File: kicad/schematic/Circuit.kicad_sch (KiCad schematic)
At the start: 54 parts, among them M1 Motor_DC, M2 Motor_DC, M3 Motor_DC, M4 Motor_DC, M5 Motor_DC, M6 Motor_DC, M7 Motor_DC, M8 Motor_DC, Q1 AO3400A, Q2 AO3400A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

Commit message: changed board layout. WIP
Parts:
- added BAT+1, BAT-1, RGB-DIN1, RGB-VDD1, RGB-gnd1, m1+1, m1-1, m2+1, m2-1, m3+1, m3-1, m4+1, m4-1, m5+1, m5-1, m6+1, m6-1, m7+1, m7-1, m8+1, m8-1: ~, ESP_global:blank pad, symbol waveshare_esp32_s3_mini_zero:blank_pad_1
- added C9: C_Polarized, Capacitor_SMD:CP_Elec_8x10.5, symbol Device:C_Polarized
- added D9: WS2812B, LED_SMD:LED_WS2812B_PLCC4_5.0x5.0mm_P3.2mm, symbol LED:WS2812B
- added H1: MountingHole_Pad, symbol Mechanical:MountingHole_Pad
- added R19: R, Resistor_SMD:R_0805_2012Metric, symbol Device:R
- added SW1: SW_Push, symbol Switch:SW_Push
- added TP1, TP2: TestPoint, symbol Connector:TestPoint
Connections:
- net GND: now also C9.2, D9.3 (VSS), RGB-gnd1.1 (pin)
- net at C1.2, C2.2, C3.2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: now also SW1.2, TP1.1, m1+1.1 (pin), m2+1.1 (pin), m3+1.1 (pin), m4+1.1 (pin), m5+1.1 (pin), m6+1.1 (pin), m7+1.1 (pin), m8+1.1 (pin); no longer U1.5 (OUT+)
- net at C2.1, D2.2 (A), M2.2 (-)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: now also m2-1.1 (pin)
- net at BT1.1 (+), U1.2 (Battery+): now also BAT+1.1 (pin)
- net at BT1.2 (-), U1.3 (Battery-): now also BAT-1.1 (pin)
- net at C8.1, D8.2 (A), M8.2 (-)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: now also m8-1.1 (pin)
- net at Q3.1 (G), R4.1: no longer R9.1
- net at C4.1, D4.2 (A), M4.2 (-)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: now also m4-1.1 (pin)
- net at ESP32_S3_ZERO1.13 (GP10), R4.2: now also R9.1
- net at Q6.1 (G), R11.1: no longer R12.1
- net at C6.1, D6.2 (A), M6.2 (-)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: now also m6-1.1 (pin)
- net at Q7.1 (G), R13.1: no longer R14.1
- net at C5.1, D5.2 (A), M5.2 (-)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: now also m5-1.1 (pin)
- net at Q4.1 (G), R5.1: no longer R10.1
- net at ESP32_S3_ZERO1.12 (GP9), R5.2: now also R10.1
- net at Q8.1 (G), R15.1: no longer R16.1
- net at ESP32_S3_ZERO1.9 (GP6), R15.2: now also R16.1
- net at Q5.1 (G), R1.1: no longer R6.1
- net at C1.1, D1.2 (A), M1.2 (-)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: now also m1-1.1 (pin)
- net at Q1.1 (G), R2.1: no longer R7.1
- net at ESP32_S3_ZERO1.15 (GP12), R2.2: now also R7.1
- net at ESP32_S3_ZERO1.1 (5V), R17.1, U2.1 (OUT_+): now also C9.1, D9.1 (VDD), RGB-VDD1.1 (pin)
- net at C7.1, D7.2 (A), M7.2 (-)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: now also m7-1.1 (pin)
- net at Q2.1 (G), R3.1: no longer R8.1
- net at C3.1, D3.2 (A), M3.2 (-)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: now also m3-1.1 (pin)
- net at ESP32_S3_ZERO1.10 (GP7), R13.2: now also R14.1
- net at ESP32_S3_ZERO1.16 (GP13), R1.2: now also R6.1
- net at ESP32_S3_ZERO1.11 (GP8), R11.2: now also R12.1
- net at ESP32_S3_ZERO1.14 (GP11), R3.2: now also R8.1
- net at ESP32_S3_ZERO1.8 (GP5): now also R19.1
- new net: D9.4 (DIN), R19.2, RGB-DIN1.1 (pin)
- new net: SW1.1, TP2.1, U1.5 (OUT+)
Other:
- moved on the sheet: ESP32_S3_ZERO1, R1, R10, R11, R12, R13, R14, R15, R16, R2, R3, R4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

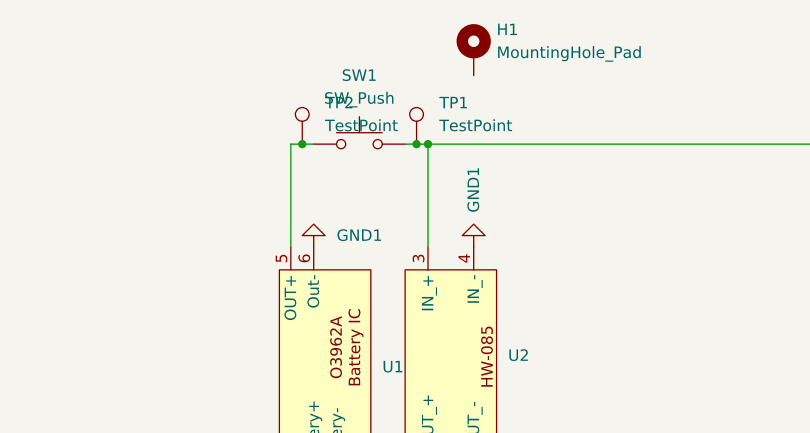
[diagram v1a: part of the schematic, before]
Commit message: upgedatetes Schematic hinzugefuegt
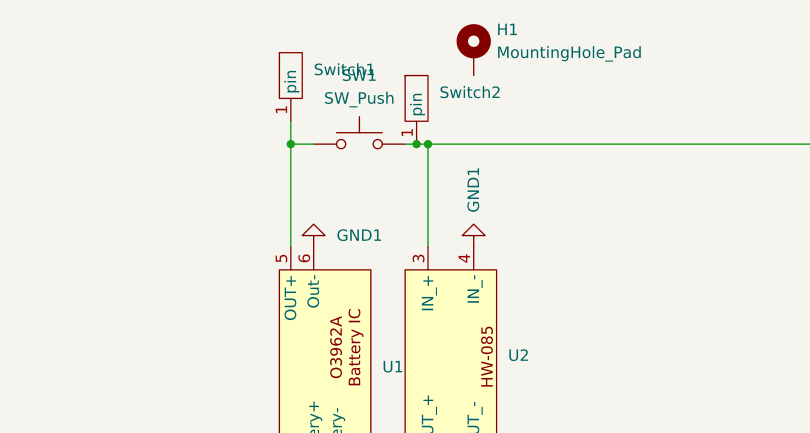
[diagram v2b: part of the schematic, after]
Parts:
- removed TP1, TP2: TestPoint, symbol Connector:TestPoint
- added Switch1, Switch2: ~, ESP_global:blank pad, symbol waveshare_esp32_s3_mini_zero:blank_pad_1
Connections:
- net at C1.2, C2.2, C3.2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: now also Switch2.1 (pin)
- net at SW1.1, U1.5 (OUT+): now also Switch1.1 (pin)
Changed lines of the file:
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@@
 	)
 	(junction
+		(at 143.51 46.99)
+		(diameter 0)
+		(color 0 0 0 0)
+	)
+	(junction
 		(at 289.56 106.68)
 		(diameter 0)
@@
 	)
 	(junction
-		(at 157.48 46.99)
-		(diameter 0)
-		(color 0 0 0 0)
-	)
-	(junction
 		(at 289.56 172.72)
 		(diameter 0)
@@
 	)
 	(junction
-		(at 144.78 46.99)
-		(diameter 0)
-		(color 0 0 0 0)
-	)
-	(junction
 		(at 234.95 182.88)
 		(diameter 0)
@@
 	)
 	(junction
+		(at 157.48 46.99)
+		(diameter 0)
+		(color 0 0 0 0)
+	)
+	(junction
 		(at 278.13 142.24)
 		(diameter 0)
@@
 	(wire
 		(pts
-			(xy 144.78 46.99) (xy 146.05 46.99)
+			(xy 143.51 46.99) (xy 146.05 46.99)
 		)
 		(stroke
@@
 	(wire
 		(pts
+			(xy 157.48 46.99) (xy 158.75 46.99)
+		)
+		(stroke
+			(width 0)
+			(type default)
+		)
+	)
+	(wire
+		(pts
 			(xy 278.13 187.96) (xy 278.13 190.5)
 		)
@@
 	(wire
 		(pts
-			(xy 143.51 46.99) (xy 144.78 46.99)
-		)
-		(stroke
-			(width 0)
-			(type default)
-		)
-	)
-	(wire
-		(pts
 			(xy 236.22 57.15) (xy 238.76 57.15)
 		)
@@
 	(wire
 		(pts
-			(xy 143.51 58.42) (xy 143.51 46.99)
-		)
-		(stroke
-			(width 0)
-			(type default)
-		)
-	)
-	(wire
-		(pts
 			(xy 278.13 71.12) (xy 278.13 73.66)
 		)
@@
 	(wire
 		(pts
+			(xy 143.51 46.99) (xy 143.51 58.42)
+		)
+		(stroke
+			(width 0)
+			(type default)
+		)
+	)
+	(wire
+		(pts
 			(xy 269.24 71.12) (xy 265.43 71.12)
 		)
@@
 	(wire
 		(pts
+			(xy 143.51 44.45) (xy 143.51 46.99)
+		)
+		(stroke
+			(width 0)
+			(type default)
+		)
+	)
+	(wire
+		(pts
 			(xy 255.27 137.16) (xy 269.24 137.16)
 		)
@@
 		)
 	)
-	(wire
-		(pts
-			(xy 157.48 46.99) (xy 158.75 46.99)
-		)
-		(stroke
-			(width 0)
-			(type default)
-		)
-	)
 	(symbol
 		(lib_id "power:GND")
@@
 	)
 	(symbol
-		(lib_id "Connector:TestPoint")
-		(at 144.78 46.99 0)
-		(unit 1)
-		(exclude_from_sim no)
-		(in_bom yes)
-		(on_board yes)
-		(dnp no)
-		(fields_autoplaced yes)
-		(property "Reference" "TP2"
-			(at 147.32 42.4179 0)
-			(effects
-				(font
-					(size 1.27 1.27)
-				)
-				(justify left)
-			)
-		)
-		(property "Value" "TestPoint"
-			(at 147.32 44.9579 0)
-			(effects
-				(font
-					(size 1.27 1.27)
-				)
-				(justify left)
-			)
-		)
-		(property "Footprint" ""
-			(at 149.86 46.99 0)
-			(effects
-				(font
-					(size 1.27 1.27)
-				)
-				(hide yes)
-			)
-		)
-		(property "Datasheet" "~"
-			(at 149.86 46.99 0)
-			(effects
-				(font
-					(size 1.27 1.27)
-				)
-				(hide yes)
-			)
-		)
-		(property "Description" "test point"
-			(at 144.78 46.99 0)
-			(effects
-				(font
-					(size 1.27 1.27)
-				)
-				(hide yes)
-			)
-		)
-		(pin "1"
-		)
-		(instances
-			(project "Circuit"
-				(path "/b1011026-c160-485a-bf1a-9bf26ac94018"
-					(reference "TP2")
-					(unit 1)
-				)
-			)
-		)
-	)
-	(symbol
 		(lib_id "Device:C")
 		(at 269.24 58.42 180)
@@
 	)
 	(symbol
+		(lib_id "waveshare_esp32_s3_mini_zero:blank_pad_1")
+		(at 143.51 39.37 0)
+		(unit 1)
+		(exclude_from_sim no)
+		(in_bom yes)
+		(on_board yes)
+		(dnp no)
+		(fields_autoplaced yes)
+		(property "Reference" "Switch1"
+			(at 146.05 38.7349 0)
+			(effects
+				(font
+					(size 1.27 1.27)
+				)
+				(justify left)
+			)
+		)
+		(property "Value" "~"
+			(at 146.05 40.64 0)
+			(effects
+				(font
+					(size 1.27 1.27)
+				)
+				(justify left)
+			)
+		)
+		(property "Footprint" "ESP_global:blank pad"
+			(at 143.51 39.37 0)
+			(effects
+				(font
+					(size 1.27 1.27)
+				)
+				(hide yes)
+			)
+		)
+		(property "Datasheet" ""
+			(at 143.51 39.37 0)
+			(effects
+				(font
+					(size 1.27 1.27)
+				)
+				(hide yes)
+			)
+		)
+		(property "Description" ""
+			(at 143.51 39.37 0)
+			(effects
+				(font
+					(size 1.27 1.27)
+				)
+				(hide yes)
+			)
+		)
+		(pin "1"
+		)
+		(instances
+			(project "Circuit"
+				(path "/b1011026-c160-485a-bf1a-9bf26ac94018"
+					(reference "Switch1")
+					(unit 1)
+				)
+			)
+		)
+	)
+	(symbol
 		(lib_id "Diode:SS14")
 		(at 278.13 95.25 270)
@@
 	)
 	(symbol
-		(lib_id "Connector:TestPoint")
-		(at 157.48 46.99 0)
-		(unit 1)
-		(exclude_from_sim no)
-		(in_bom yes)
-		(on_board yes)
-		(dnp no)
-		(fields_autoplaced yes)
-		(property "Reference" "TP1"
-			(at 160.02 42.4179 0)
-			(effects
-				(font
-					(size 1.27 1.27)
-				)
-				(justify left)
-			)
-		)
-		(property "Value" "TestPoint"
-			(at 160.02 44.9579 0)
-			(effects
-				(font
-					(size 1.27 1.27)
-				)
-				(justify left)
-			)
-		)
-		(property "Footprint" ""
-			(at 162.56 46.99 0)
-			(effects
-				(font
-					(size 1.27 1.27)
-				)
-				(hide yes)
-			)
-		)
-		(property "Datasheet" "~"
-			(at 162.56 46.99 0)
-			(effects
-				(font
-					(size 1.27 1.27)
-				)
-				(hide yes)
-			)
-		)
-		(property "Description" "test point"
-			(at 157.48 46.99 0)
-			(effects
-				(font
-					(size 1.27 1.27)
-				)
-				(hide yes)
-			)
-		)
-		(pin "1"
-		)
-		(instances
-			(project ""
-				(path "/b1011026-c160-485a-bf1a-9bf26ac94018"
-					(reference "TP1")
-					(unit 1)
-				)
-			)
-		)
-	)
-	(symbol
 		(lib_id "power:GND")
 		(at 231.14 83.82 270)
@@
 					(unit 1)
 				)
+			)
+		)
+	)
+	(symbol
+		(lib_id "waveshare_esp32_s3_mini_zero:blank_pad_1")
+		(at 157.48 41.91 0)
+		(unit 1)
+		(exclude_from_sim no)
+		(in_bom yes)
+		(on_board yes)
+		(dnp no)
+		(fields_autoplaced yes)
+		(property "Reference" "Switch2"
+			(at 160.02 41.2749 0)
+			(effects
+				(font
+					(size 1.27 1.27)
+				)
+				(justify left)
+			)
+		)
+		(property "Value" "~"
+			(at 160.02 43.18 0)
+			(effects
+				(font
+					(size 1.27 1.27)
+				)
+				(justify left)
+			)
+		)
+		(property "Footprint" "ESP_global:blank pad"
+			(at 157.48 41.91 0)
+			(effects
+				(font
+					(size 1.27 1.27)
+				)
+				(hide yes)
+			)
+		)
+		(property "Datasheet" ""
+			(at 157.48 41.91 0)
+			(effects
+				(font
+					(size 1.27 1.27)
+				)
+				(hide yes)
+			)
+		)
+		(property "Description" ""
+			(at 157.48 41.91 0)
+			(effects
+				(font
+					(size 1.27 1.27)
+				)
+				(hide yes)
+			)
+		)
+		(pin "1"
+		)
+		(instances
+			(project "Circuit"
+				(path "/b1011026-c160-485a-bf1a-9bf26ac94018"
+					(reference "Switch2")
+					(unit 1)
+				)

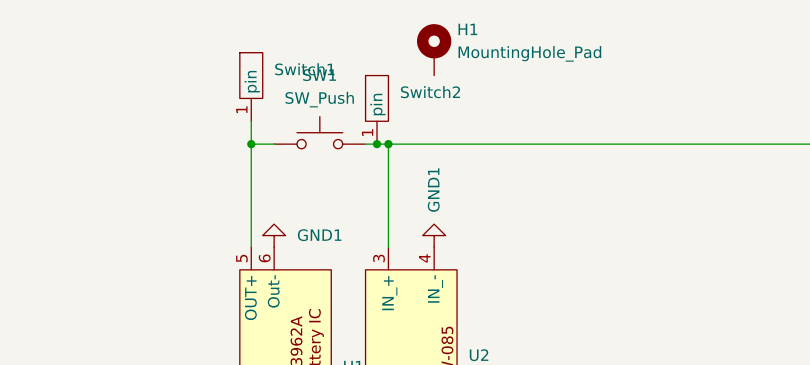
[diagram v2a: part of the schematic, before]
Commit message: fixed board size beschriftungen verbessert
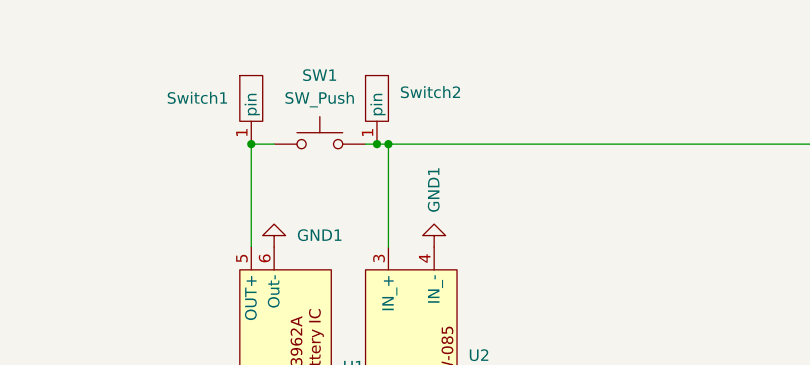
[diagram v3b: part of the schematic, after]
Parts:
- removed H1: MountingHole_Pad, symbol Mechanical:MountingHole_Pad
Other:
- moved on the sheet: Switch1
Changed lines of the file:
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@@
 	(wire
 		(pts
-			(xy 143.51 44.45) (xy 143.51 46.99)
-		)
-		(stroke
-			(width 0)
-			(type default)
-		)
-	)
-	(wire
-		(pts
 			(xy 255.27 137.16) (xy 269.24 137.16)
 		)
@@
 	)
 	(symbol
-		(lib_id "Mechanical:MountingHole_Pad")
-		(at 163.83 36.83 0)
-		(unit 1)
-		(exclude_from_sim no)
-		(in_bom yes)
-		(on_board yes)
-		(dnp no)
-		(fields_autoplaced yes)
-		(property "Reference" "H1"
-			(at 166.37 34.2899 0)
-			(effects
-				(font
-					(size 1.27 1.27)
-				)
-				(justify left)
-			)
-		)
-		(property "Value" "MountingHole_Pad"
-			(at 166.37 36.8299 0)
-			(effects
-				(font
-					(size 1.27 1.27)
-				)
-				(justify left)
-			)
-		)
-		(property "Footprint" ""
-			(at 163.83 36.83 0)
-			(effects
-				(font
-					(size 1.27 1.27)
-				)
-				(hide yes)
-			)
-		)
-		(property "Datasheet" "~"
-			(at 163.83 36.83 0)
-			(effects
-				(font
-					(size 1.27 1.27)
-				)
-				(hide yes)
-			)
-		)
-		(property "Description" "Mounting Hole with connection"
-			(at 163.83 36.83 0)
-			(effects
-				(font
-					(size 1.27 1.27)
-				)
-				(hide yes)
-			)
-		)
-		(pin "1"
-		)
-		(instances
-			(project ""
-				(path "/b1011026-c160-485a-bf1a-9bf26ac94018"
-					(reference "H1")
-					(unit 1)
-				)
-			)
-		)
-	)
-	(symbol
 		(lib_id "Diode:SS14")
 		(at 278.13 77.47 270)
@@
 	(symbol
 		(lib_id "waveshare_esp32_s3_mini_zero:blank_pad_1")
-		(at 143.51 39.37 0)
+		(at 143.51 41.91 0)
 		(unit 1)
 		(exclude_from_sim no)
@@
 		(on_board yes)
 		(dnp no)
-		(fields_autoplaced yes)
 		(property "Reference" "Switch1"
-			(at 146.05 38.7349 0)
+			(at 134.112 41.91 0)
 			(effects
 				(font
@@
 		)
 		(property "Value" "~"
-			(at 146.05 40.64 0)
+			(at 146.05 43.18 0)
 			(effects
 				(font
@@
 		)
 		(property "Footprint" "ESP_global:blank pad"
-			(at 143.51 39.37 0)
+			(at 143.51 41.91 0)
 			(effects
 				(font
@@
 		)
 		(property "Datasheet" ""
-			(at 143.51 39.37 0)
+			(at 143.51 41.91 0)
 			(effects
 				(font
@@
 		)
 		(property "Description" ""
-			(at 143.51 39.37 0)
+			(at 143.51 41.91 0)
 			(effects
 				(font

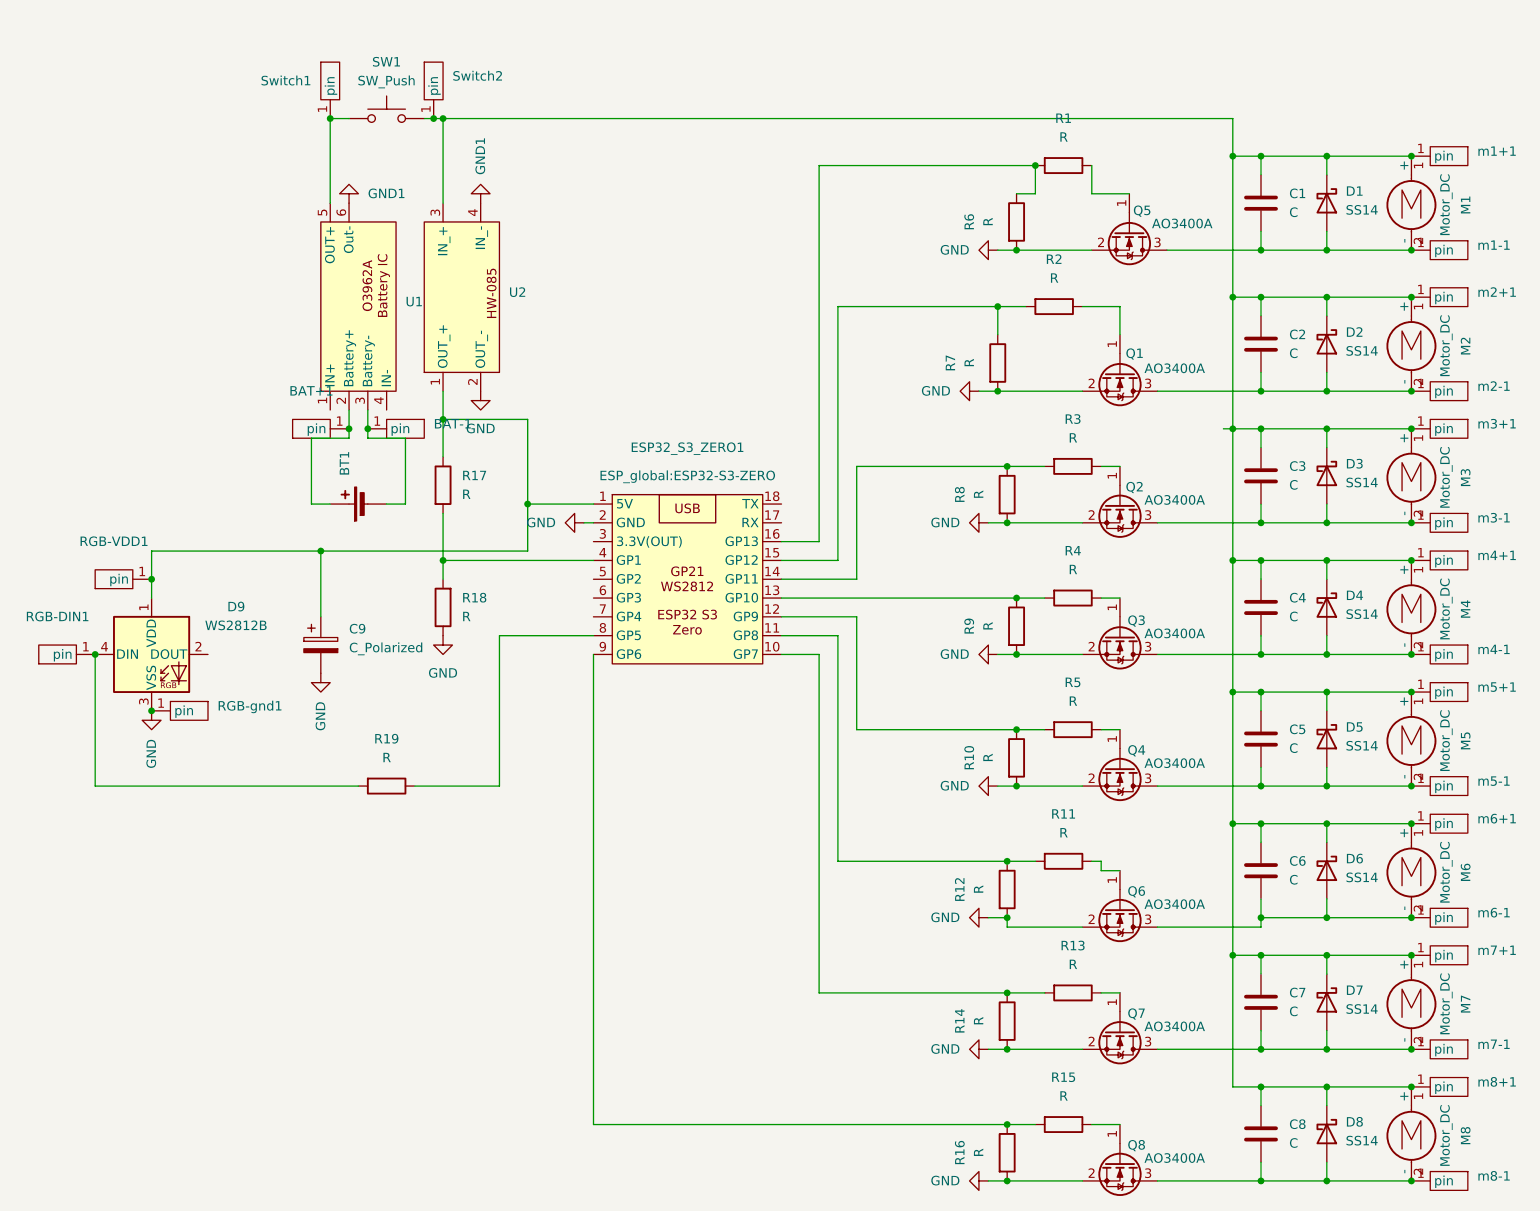
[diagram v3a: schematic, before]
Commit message: changed pads HW-085
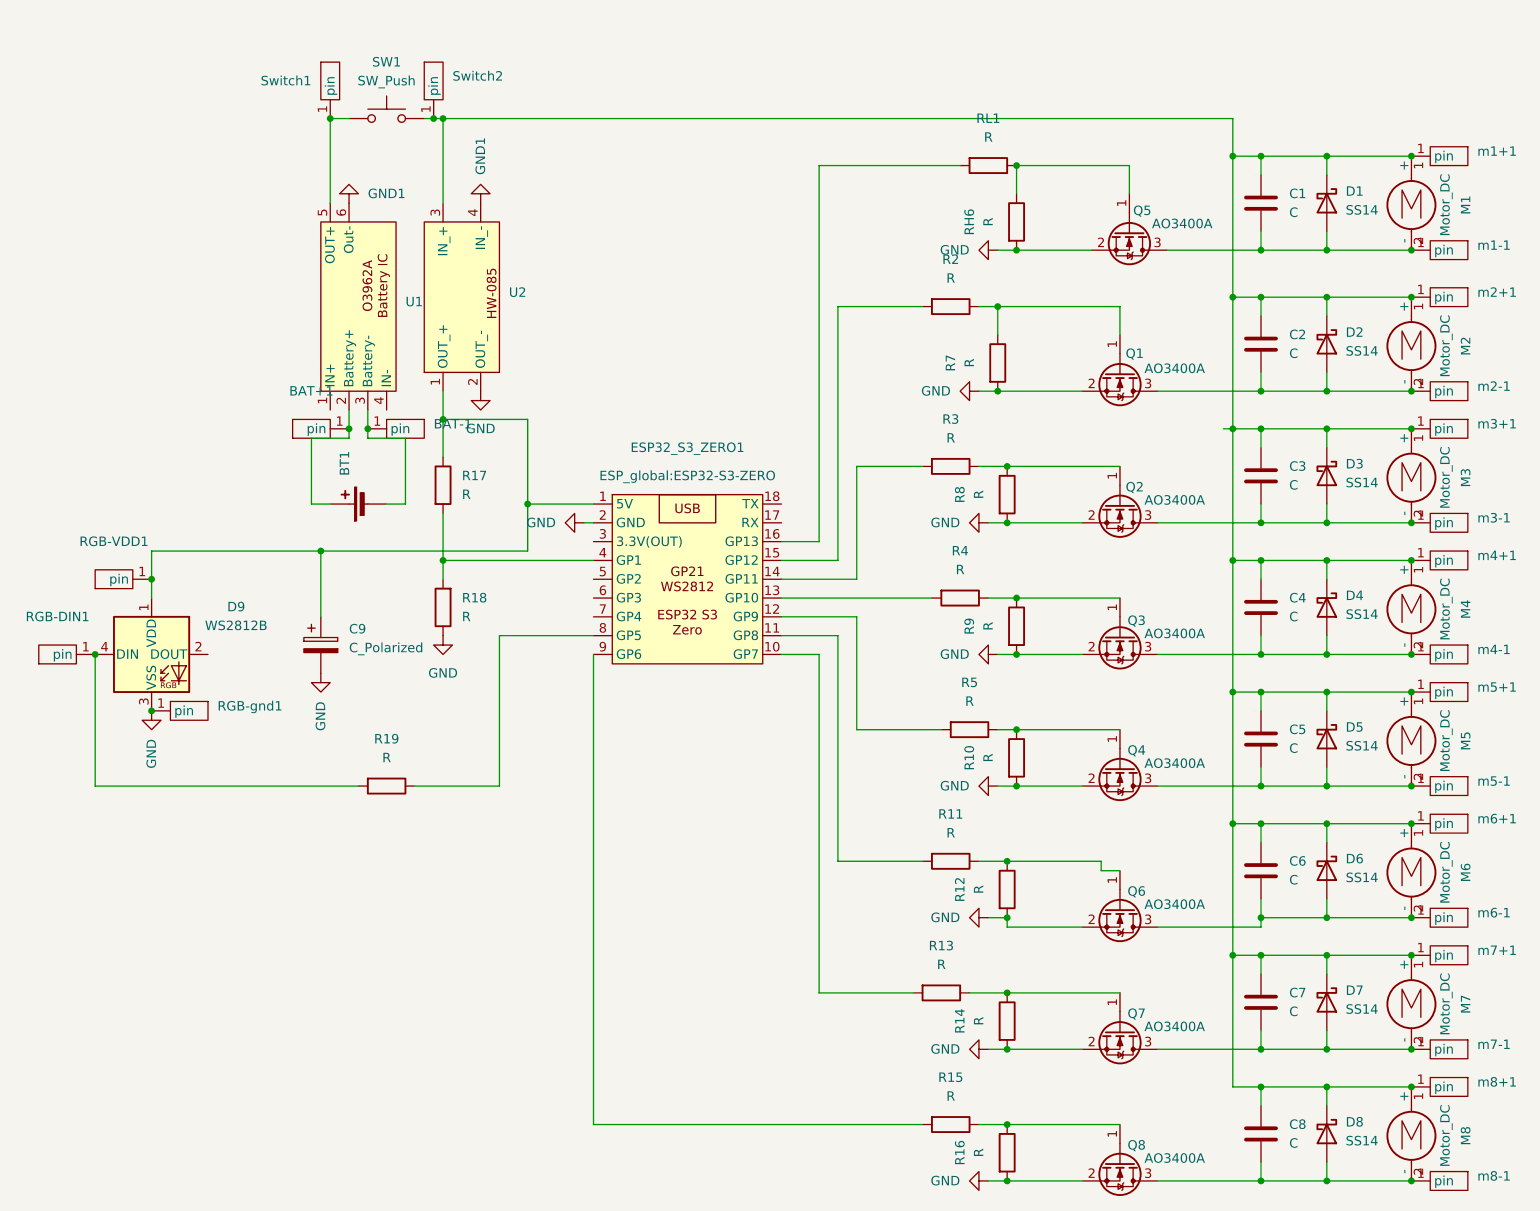
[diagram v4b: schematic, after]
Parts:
- renumbered R6 to RH6, R1 to RL1
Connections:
- net at Q3.1 (G), R4.1: now also R9.1
- net at ESP32_S3_ZERO1.13 (GP10), R4.2: no longer R9.1
- net at Q6.1 (G), R11.1: now also R12.1
- net at ESP32_S3_ZERO1.10 (GP7), R13.2: no longer R14.1
- net at Q4.1 (G), R5.1: now also R10.1
- net at ESP32_S3_ZERO1.12 (GP9), R5.2: no longer R10.1
- net at Q8.1 (G), R15.1: now also R16.1
- net at ESP32_S3_ZERO1.9 (GP6), R15.2: no longer R16.1
- net at ESP32_S3_ZERO1.11 (GP8), R11.2: no longer R12.1
- net at Q5.1 (G), RL1.1: now also RH6.1
- net at Q1.1 (G), R2.1: now also R7.1
- net at ESP32_S3_ZERO1.15 (GP12), R2.2: no longer R7.1
- net at ESP32_S3_ZERO1.14 (GP11), R3.2: no longer R8.1
- net at ESP32_S3_ZERO1.16 (GP13), RL1.2: no longer RH6.1
- net at Q7.1 (G), R13.1: now also R14.1
- net at Q2.1 (G), R3.1: now also R8.1
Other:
- moved on the sheet: R11, R13, R15, R2, R3, R4, R5, RL1
